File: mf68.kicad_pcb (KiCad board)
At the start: 2 copper layers, 2 parts, among them SW1 MX, U1 nice_nano

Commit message: Arranged a large amount of switches
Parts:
- removed SW1: MX, Keebio-Parts:MX-Alps-Choc-1U
- added D1: D, Diode_THT:D_DO-34_SOD68_P10.16mm_Horizontal, B.Cu at (34.9, -53.2)
- added D10: D, Diode_THT:D_DO-34_SOD68_P10.16mm_Horizontal, B.Cu at (206.4, -53.2)
- added D11: D, Diode_THT:D_DO-34_SOD68_P10.16mm_Horizontal, B.Cu at (225.4, -53.2)
- added D12: D, Diode_THT:D_DO-34_SOD68_P10.16mm_Horizontal, B.Cu at (244.5, -53.2)
- added D13: D, Diode_THT:D_DO-34_SOD68_P10.16mm_Horizontal, B.Cu at (263.5, -53.2)
- added D14: D, Diode_THT:D_DO-34_SOD68_P10.16mm_Horizontal, B.Cu at (42.1, -34.1)
- added D15: D, Diode_THT:D_DO-34_SOD68_P10.16mm_Horizontal, B.Cu at (63.5, -34.1)
- added D16: D, Diode_THT:D_DO-34_SOD68_P10.16mm_Horizontal, B.Cu at (82.5, -34.1)
- added D17: D, Diode_THT:D_DO-34_SOD68_P10.16mm_Horizontal, B.Cu at (101.6, -34.1)
- added D18: D, Diode_THT:D_DO-34_SOD68_P10.16mm_Horizontal, B.Cu at (120.6, -34.1)
- added D19: D, Diode_THT:D_DO-34_SOD68_P10.16mm_Horizontal, B.Cu at (139.7, -34.1)
- added D2: D, Diode_THT:D_DO-34_SOD68_P10.16mm_Horizontal, B.Cu at (54.0, -53.2)
- added D20: D, Diode_THT:D_DO-34_SOD68_P10.16mm_Horizontal, B.Cu at (158.7, -34.1)
- added D21: D, Diode_THT:D_DO-34_SOD68_P10.16mm_Horizontal, B.Cu at (177.8, -34.1)
- added D22: D, Diode_THT:D_DO-34_SOD68_P10.16mm_Horizontal, B.Cu at (196.8, -34.1)
- added D23: D, Diode_THT:D_DO-34_SOD68_P10.16mm_Horizontal, B.Cu at (215.9, -34.1)
- added D24: D, Diode_THT:D_DO-34_SOD68_P10.16mm_Horizontal, B.Cu at (234.9, -34.1)
- added D25: D, Diode_THT:D_DO-34_SOD68_P10.16mm_Horizontal, B.Cu at (254.0, -34.1)
- added D26: D, Diode_THT:D_DO-34_SOD68_P10.16mm_Horizontal, B.Cu at (273.0, -34.1)
- added D27: D, Diode_THT:D_DO-34_SOD68_P10.16mm_Horizontal, B.Cu at (44.4, -15.1)
- added D28: D, Diode_THT:D_DO-34_SOD68_P10.16mm_Horizontal, B.Cu at (68.3, -15.1)
- added D29: D, Diode_THT:D_DO-34_SOD68_P10.16mm_Horizontal, B.Cu at (87.3, -15.1)
- added D3: D, Diode_THT:D_DO-34_SOD68_P10.16mm_Horizontal, B.Cu at (73.8, -53.2)
- added D30: D, Diode_THT:D_DO-34_SOD68_P10.16mm_Horizontal, B.Cu at (106.4, -15.1)
- added D31: D, Diode_THT:D_DO-34_SOD68_P10.16mm_Horizontal, B.Cu at (111.9, -8.73)
- added D32: D, Diode_THT:D_DO-34_SOD68_P10.16mm_Horizontal, F.Cu at (131.0, -11.9)
- added D33: D, Diode_THT:D_DO-34_SOD68_P10.16mm_Horizontal, F.Cu at (150.0, -11.9)
- added D34: D, Diode_THT:D_DO-34_SOD68_P10.16mm_Horizontal, F.Cu at (169.1, -11.9)
- added D35: D, Diode_THT:D_DO-34_SOD68_P10.16mm_Horizontal, F.Cu at (188.1, -11.9)
- added D36: D, Diode_THT:D_DO-34_SOD68_P10.16mm_Horizontal, F.Cu at (207.2, -11.9)
- added D37: D, Diode_THT:D_DO-34_SOD68_P10.16mm_Horizontal, F.Cu at (226.2, -11.9)
- added D38: D, Diode_THT:D_DO-34_SOD68_P10.16mm_Horizontal, F.Cu at (245.3, -11.9)
- added D39: D, Diode_THT:D_DO-34_SOD68_P10.16mm_Horizontal, F.Cu at (276.2, -11.9)
- added D4: D, Diode_THT:D_DO-34_SOD68_P10.16mm_Horizontal, B.Cu at (92.1, -53.2)
- added D40: D, Diode_THT:D_DO-34_SOD68_P10.16mm_Horizontal, F.Cu at (27.0, 5.56)
- added D41: D, Diode_THT:D_DO-34_SOD68_P10.16mm_Horizontal, F.Cu at (63.5, 5.56)
- added D42: D, Diode_THT:D_DO-34_SOD68_P10.16mm_Horizontal, F.Cu at (83.3, 5.56)
- added D43: D, Diode_THT:D_DO-34_SOD68_P10.16mm_Horizontal, F.Cu at (101.6, 5.56)
- added D44: D, Diode_THT:D_DO-34_SOD68_P10.16mm_Horizontal, F.Cu at (120.6, 5.56)
- added D45: D, Diode_THT:D_DO-34_SOD68_P10.16mm_Horizontal, F.Cu at (139.7, 5.56)
- added D46: D, Diode_THT:D_DO-34_SOD68_P10.16mm_Horizontal, F.Cu at (158.7, 5.56)
- added D47: D, Diode_THT:D_DO-34_SOD68_P10.16mm_Horizontal, F.Cu at (177.8, 5.56)
- added D48: D, Diode_THT:D_DO-34_SOD68_P10.16mm_Horizontal, F.Cu at (196.8, 5.56)
- added D49: D, Diode_THT:D_DO-34_SOD68_P10.16mm_Horizontal, F.Cu at (215.9, 5.56)
- added D5: D, Diode_THT:D_DO-34_SOD68_P10.16mm_Horizontal, B.Cu at (111.1, -53.2)
- added D50: D, Diode_THT:D_DO-34_SOD68_P10.16mm_Horizontal, F.Cu at (234.9, 5.56)
- added D51: D, Diode_THT:D_DO-34_SOD68_P10.16mm_Horizontal, F.Cu at (254.0, 5.56)
- added D52: D, Diode_THT:D_DO-34_SOD68_P10.16mm_Horizontal, B.Cu at (280.2, -44.4)
- added D53: D, Diode_THT:D_DO-34_SOD68_P10.16mm_Horizontal, F.Cu at (29.4, 26.2)
- added D54: D, Diode_THT:D_DO-34_SOD68_P10.16mm_Horizontal, F.Cu at (53.2, 26.2)
- added D55: D, Diode_THT:D_DO-34_SOD68_P10.16mm_Horizontal, F.Cu at (77.0, 26.2)
- added D56: D, Diode_THT:D_DO-34_SOD68_P10.16mm_Horizontal, F.Cu at (100.8, 26.2)
- added D57: D, Diode_THT:D_DO-34_SOD68_P10.16mm_Horizontal, F.Cu at (138.9, 26.2)
- added D58: D, Diode_THT:D_DO-34_SOD68_P10.16mm_Horizontal, F.Cu at (179.4, 26.2)
- added D59: D, Diode_THT:D_DO-34_SOD68_P10.16mm_Horizontal, F.Cu at (218.3, 26.2)
- added D6: D, Diode_THT:D_DO-34_SOD68_P10.16mm_Horizontal, B.Cu at (130.2, -53.2)
- added D60: D, Diode_THT:D_DO-34_SOD68_P10.16mm_Horizontal, F.Cu at (241.3, 26.2)
- added D61: D, Diode_THT:D_DO-34_SOD68_P10.16mm_Horizontal, F.Cu at (265.9, 26.2)
- added D62: D, Diode_THT:D_DO-34_SOD68_P10.16mm_Horizontal, F.Cu at (284.9, 26.2)
- added D63: D, Diode_THT:D_DO-34_SOD68_P10.16mm_Horizontal, F.Cu at (304.0, 26.2)
- added D64: D, Diode_THT:D_DO-34_SOD68_P10.16mm_Horizontal, F.Cu at (284.9, 7.14)
- added D65: D, Diode_THT:D_DO-34_SOD68_P10.16mm_Horizontal, F.Cu at (275.4, -54.0)
- added D7: D, Diode_THT:D_DO-34_SOD68_P10.16mm_Horizontal, B.Cu at (149.2, -53.2)
- added D8: D, Diode_THT:D_DO-34_SOD68_P10.16mm_Horizontal, B.Cu at (168.3, -53.2)
- added D9: D, Diode_THT:D_DO-34_SOD68_P10.16mm_Horizontal, B.Cu at (187.3, -53.2)
- added K1: ESC, Keebio-Parts:MX-Alps-Choc-1U-NoLED, F.Cu at (25.4, -59.5)
- added K10: #9, Keebio-Parts:MX-Alps-Choc-1U-NoLED, F.Cu at (196.8, -59.5)
- added K11: #0, Keebio-Parts:MX-Alps-Choc-1U-NoLED, F.Cu at (215.9, -59.5)
- added K12: MINUS, Keebio-Parts:MX-Alps-Choc-1U-NoLED, F.Cu at (234.9, -59.5)
- added K13: PLUS, Keebio-Parts:MX-Alps-Choc-1U-NoLED, F.Cu at (254.0, -59.5)
- added K14: TAB, Keebio-Parts:MX-Alps-Choc-1U-NoLED, F.Cu at (30.2, -40.5)
- added K15: Q, Keebio-Parts:MX-Alps-Choc-1U-NoLED, F.Cu at (54.0, -40.5)
- added K16: W, Keebio-Parts:MX-Alps-Choc-1U-NoLED, F.Cu at (73.0, -40.5)
- added K17: E, Keebio-Parts:MX-Alps-Choc-1U-NoLED, F.Cu at (92.1, -40.5)
- added K18: R, Keebio-Parts:MX-Alps-Choc-1U-NoLED, F.Cu at (111.1, -40.5)
- added K19: T, Keebio-Parts:MX-Alps-Choc-1U-NoLED, F.Cu at (130.2, -40.5)
- added K2: #1, Keebio-Parts:MX-Alps-Choc-1U-NoLED, F.Cu at (44.4, -59.5)
- added K20: Y, Keebio-Parts:MX-Alps-Choc-1U-NoLED, F.Cu at (149.2, -40.5)
- added K21: U, Keebio-Parts:MX-Alps-Choc-1U-NoLED, F.Cu at (168.3, -40.5)
- added K22: I, Keebio-Parts:MX-Alps-Choc-1U-NoLED, F.Cu at (187.3, -40.5)
- added K23: O, Keebio-Parts:MX-Alps-Choc-1U-NoLED, F.Cu at (206.4, -40.5)
- added K24: P, Keebio-Parts:MX-Alps-Choc-1U-NoLED, F.Cu at (225.4, -40.5)
- added K25: [, Keebio-Parts:MX-Alps-Choc-1U-NoLED, F.Cu at (244.5, -40.5)
- added K26: ], Keebio-Parts:MX-Alps-Choc-1U-NoLED, F.Cu at (263.5, -40.5)
- added K27: CAPS, Keebio-Parts:MX-Alps-Choc-1U-NoLED, F.Cu at (34.9, -21.4)
- added K28: A, Keebio-Parts:MX-Alps-Choc-1U-NoLED, F.Cu at (58.7, -21.4)
- added K29: S, Keebio-Parts:MX-Alps-Choc-1U-NoLED, F.Cu at (77.8, -21.4)
- added K3: #2, Keebio-Parts:MX-Alps-Choc-1U-NoLED, F.Cu at (63.5, -59.5)
- added K30: D, Keebio-Parts:MX-Alps-Choc-1U-NoLED, F.Cu at (96.8, -21.4)
- added K31: F, Keebio-Parts:MX-Alps-Choc-1U-NoLED, F.Cu at (115.9, -21.4)
- added K32: G, Keebio-Parts:MX-Alps-Choc-1U-NoLED, F.Cu at (134.9, -21.4)
- added K33: H, Keebio-Parts:MX-Alps-Choc-1U-NoLED, F.Cu at (154.0, -21.4)
- added K34: J, Keebio-Parts:MX-Alps-Choc-1U-NoLED, F.Cu at (173.0, -21.4)
- added K35: K, Keebio-Parts:MX-Alps-Choc-1U-NoLED, F.Cu at (192.1, -21.4)
- added K36: L, Keebio-Parts:MX-Alps-Choc-1U-NoLED, F.Cu at (211.1, -21.4)
- added K37: ;, Keebio-Parts:MX-Alps-Choc-1U-NoLED, F.Cu at (230.2, -21.4)
- added K38: ', Keebio-Parts:MX-Alps-Choc-1U-NoLED, F.Cu at (249.2, -21.4)
- added K39: ENTER, Keebio-Parts:MX-Alps-Choc-1U-NoLED, F.Cu at (281.0, -21.4)
- added K4: #3, Keebio-Parts:MX-Alps-Choc-1U-NoLED, F.Cu at (82.5, -59.5)
- added K40: LSHIFT, Keebio-Parts:MX-Alps-Choc-1U-NoLED, F.Cu at (31.7, -2.38)
- added K41: Z, Keebio-Parts:MX-Alps-Choc-1U-NoLED, F.Cu at (68.3, -2.38)
- added K42: X, Keebio-Parts:MX-Alps-Choc-1U-NoLED, F.Cu at (87.3, -2.38)
- added K43: C, Keebio-Parts:MX-Alps-Choc-1U-NoLED, F.Cu at (106.4, -2.38)
- added K44: V, Keebio-Parts:MX-Alps-Choc-1U-NoLED, F.Cu at (125.4, -2.38)
- added K45: B, Keebio-Parts:MX-Alps-Choc-1U-NoLED, F.Cu at (144.5, -2.38)
- added K46: N, Keebio-Parts:MX-Alps-Choc-1U-NoLED, F.Cu at (163.5, -2.38)
- added K47: M, Keebio-Parts:MX-Alps-Choc-1U-NoLED, F.Cu at (182.6, -2.38)
- added K48: ,, Keebio-Parts:MX-Alps-Choc-1U-NoLED, F.Cu at (201.6, -2.38)
- added K49: ., Keebio-Parts:MX-Alps-Choc-1U-NoLED, F.Cu at (220.6, -2.38)
- added K5: #4, Keebio-Parts:MX-Alps-Choc-1U-NoLED, F.Cu at (101.6, -59.5)
- added K50: /, Keebio-Parts:MX-Alps-Choc-1U-NoLED, F.Cu at (239.7, -2.38)
- added K51: RSHIFT, Keebio-Parts:MX-Alps-Choc-1U-NoLED, F.Cu at (258.7, -2.38)
- added K52: BKSH, Keebio-Parts:MX-Alps-Choc-1U-NoLED, F.Cu at (289.7, -40.5)
- added K53: LCTL, Keebio-Parts:MX-Alps-Choc-1U-NoLED, F.Cu at (34.1, 16.7)
- added K54: LWIN, Keebio-Parts:MX-Alps-Choc-1U-NoLED, F.Cu at (57.9, 16.7)
- added K55: LALT, Keebio-Parts:MX-Alps-Choc-1U-NoLED, F.Cu at (81.8, 16.7)
- added K56: FN2, Keebio-Parts:MX-Alps-Choc-1U-NoLED, F.Cu at (105.6, 16.7)
- added K57: LSPC, Keebio-Parts:MX-Alps-Choc-1U-NoLED, F.Cu at (143.7, 16.7)
- added K58: RSPC, Keebio-Parts:MX-Alps-Choc-1U-NoLED, F.Cu at (184.1, 16.7)
- added K59: RALT, Keebio-Parts:MX-Alps-Choc-1U-NoLED, F.Cu at (223.0, 16.7)
- added K6: #5, Keebio-Parts:MX-Alps-Choc-1U-NoLED, F.Cu at (120.6, -59.5)
- added K60: RGUI, Keebio-Parts:MX-Alps-Choc-1U-NoLED, F.Cu at (246.0, 16.7)
- added K61: LEFT, Keebio-Parts:MX-Alps-Choc-1U-NoLED, F.Cu at (270.7, 16.7)
- added K62: DOWN, Keebio-Parts:MX-Alps-Choc-1U-NoLED, F.Cu at (289.7, 16.7)
- added K63: RIGHT, Keebio-Parts:MX-Alps-Choc-1U-NoLED, F.Cu at (308.7, 16.7)
- added K64: UP, Keebio-Parts:MX-Alps-Choc-1U-NoLED, F.Cu at (289.7, -2.38)
- added K65: BKSPC, Keebio-Parts:MX-Alps-Choc-1U-NoLED, F.Cu at (289.7, -59.5)
- added K7: #6, Keebio-Parts:MX-Alps-Choc-1U-NoLED, F.Cu at (139.7, -59.5)
- added K8: #7, Keebio-Parts:MX-Alps-Choc-1U-NoLED, F.Cu at (158.7, -59.5)
- added K9: #8, Keebio-Parts:MX-Alps-Choc-1U-NoLED, F.Cu at (177.8, -59.5)
- U1: moved to B.Cu
- moved U1 245.2 mm to (311.1, -51.6), turned to 270 degrees
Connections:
- U1 pad 1: (no net) -> row0
- U1 pad 10: (no net) -> col10
- U1 pad 11: (no net) -> col11
- U1 pad 12: (no net) -> col12
- U1 pad 13: (no net) -> col7
- U1 pad 14: (no net) -> col6
- U1 pad 15: (no net) -> col5
- U1 pad 16: (no net) -> col4
- U1 pad 17: (no net) -> col3
- U1 pad 18: (no net) -> col2
- U1 pad 19: (no net) -> col1
- U1 pad 2: (no net) -> row1
- U1 pad 20: (no net) -> col0
- U1 pad 5: (no net) -> row2
- U1 pad 6: (no net) -> row3
- U1 pad 7: (no net) -> row4
- U1 pad 8: (no net) -> col8
- U1 pad 9: (no net) -> col9
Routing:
- net row0: track 0.00 -> 372.1 mm
- net row1: track 0.00 -> 349.4 mm
- net (no net): track 0.00 -> 71.7 mm
- net col0: track 0.00 -> 58.5 mm
- net Net-(D3-Pad2): track 0.00 -> 8.11 mm
- net Net-(D13-Pad2): track 0.00 -> 7.32 mm
- net Net-(D5-Pad2): track 0.00 -> 7.32 mm
- net Net-(D4-Pad2): track 0.00 -> 7.32 mm
- net Net-(D1-Pad2): track 0.00 -> 7.32 mm
- net Net-(D6-Pad2): track 0.00 -> 7.32 mm
- net Net-(D2-Pad2): track 0.00 -> 7.32 mm
- net Net-(D9-Pad2): track 0.00 -> 7.32 mm
- net Net-(D8-Pad2): track 0.00 -> 7.32 mm
- net Net-(D7-Pad2): track 0.00 -> 7.32 mm
- net Net-(D12-Pad2): track 0.00 -> 7.32 mm
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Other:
- net class Default: trace_width 0.25 -> 0.4

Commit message: Wip: row stagger is wrong!
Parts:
- added REF**: 1.25U, MX_Alps_Hybrid:MX-1.25U, F.Cu at (273.0, 148.4)
- added REF**: 1.25U, MX_Alps_Hybrid:MX-1.25U, F.Cu at (249.2, 148.4)
- added REF**: 1.25U, MX_Alps_Hybrid:MX-1.25U, F.Cu at (225.4, 148.4)
- added REF**: 1.25U, MX_Alps_Hybrid:MX-1.25U, F.Cu at (201.6, 148.4)
- added REF**: 1.25U, MX_Alps_Hybrid:MX-1.25U, F.Cu at (58.7, 148.4)
- added REF**: 1.25U, MX_Alps_Hybrid:MX-1.25U, F.Cu at (34.9, 148.4)
- added REF**: 1.25U, MX_Alps_Hybrid:MX-1.25U, F.Cu at (11.1, 148.4)
- added REF**: 6.25U, MX_Alps_Hybrid:MX-6.25U, F.Cu at (130.2, 148.4)
- D32, D33, D34, D35, D36, D37, D38, D39, D40, D41, D42, D43, D44, D45, D46, D47, D48, D49, D50, D51, D53, D54, D55, D56, D57, D58, D59, D60, D61, D62, D63, D64, D65: moved to B.Cu
- K39, K57, K58: footprint Keebio-Parts:MX-Alps-Choc-1U-NoLED -> Keebio-Parts:MX-Alps-Choc-2U
- K40: footprint Keebio-Parts:MX-Alps-Choc-1U-NoLED -> xeal_components:MX-Alps-Choc-2U-pin-flip
- K61, K62, K63: footprint Keebio-Parts:MX-Alps-Choc-1U-NoLED -> xeal_components:MX-Alps-Choc-1U-NoLED-PinSwap
- K65: footprint Keebio-Parts:MX-Alps-Choc-1U-NoLED -> xeal_components:MX-Alps-Choc-2U-no-led
- moved K57 116.1 mm to (115.9, 129.4), turned to 180 degrees
- moved K53 115.0 mm to (11.1, 129.4)
- moved K54 115.0 mm to (34.9, 129.4)
- moved K55 115.0 mm to (58.7, 129.4)
- moved K56 115.0 mm to (82.5, 129.4)
- moved K59 114.7 mm to (201.6, 129.4)
- moved K65 114.7 mm to (268.3, 53.2)
- moved K58 114.6 mm to (163.5, 129.4), turned to 180 degrees
- moved K60 114.6 mm to (225.4, 129.4)
- moved K39 113.7 mm to (265.9, 91.3)
- moved D65 113.6 mm to (251.6, 57.1)
- moved K1 113.6 mm to (11.1, 53.2)
- moved K10 113.6 mm to (182.6, 53.2)
- moved K11 113.6 mm to (201.6, 53.2)
- moved K12 113.6 mm to (220.6, 53.2)
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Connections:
- U1 pad 1: row0 -> row1
- U1 pad 10: col10 -> col12
- U1 pad 12: col12 -> row3
- U1 pad 13: col7 -> col6
- U1 pad 14: col6 -> col5
- U1 pad 15: col5 -> col4
- U1 pad 16: col4 -> col3
- U1 pad 17: col3 -> col2
- U1 pad 18: col2 -> col1
- U1 pad 19: col1 -> col0
- U1 pad 2: row1 -> col7
- U1 pad 20: col0 -> row0
- U1 pad 6: row3 -> col8
- U1 pad 7: row4 -> col9
- U1 pad 8: col8 -> col10
- U1 pad 9: col9 -> row4
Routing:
- net row4: track 0.00 -> 504.2 mm, vias 0 -> 1
- net row3: track 0.00 -> 399.4 mm
- net col1: track 0.00 -> 384.1 mm
- net col2: track 0.00 -> 358.3 mm, vias 0 -> 1
- net col7: track 0.00 -> 349.0 mm
- net row2: track 0.00 -> 343.8 mm, vias 0 -> 1
- net col3: track 0.00 -> 336.9 mm, vias 0 -> 1
- net col8: track 0.00 -> 330.5 mm
- net col4: track 0.00 -> 328.1 mm, vias 0 -> 1
- net col6: track 0.00 -> 325.4 mm, vias 0 -> 1
- net col5: track 0.00 -> 319.6 mm, vias 0 -> 1
- net col0: track 58.5 -> 376.5 mm
- net col9: track 0.00 -> 310.9 mm
- net col10: track 0.00 -> 291.8 mm
- net col12: track 0.00 -> 189.2 mm
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
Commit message: wip: Row stagger fixed for ansi
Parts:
- removed the REF** at (273.0, 148.4)
- removed the REF** at (249.2, 148.4)
- removed the REF** at (225.4, 148.4)
- removed the REF** at (201.6, 148.4)
- removed the REF** at (58.7, 148.4)
- removed the REF** at (34.9, 148.4)
- added REF**: 1.75U, MX_Alps_Hybrid:MX-1.75U, F.Cu at (251.6, 110.3)
- added REF**: 1.25U, MX_Alps_Hybrid:MX-1.25U, F.Cu at (37.3, 148.4)
- added REF**: 1.5U, MX_Alps_Hybrid:MX-1.5U, F.Cu at (65.1, 185.7)
- added REF**: 1.5U, MX_Alps_Hybrid:MX-1.5U, F.Cu at (36.5, 185.7)
- added REF**: 1.25U, MX_Alps_Hybrid:MX-1.25U, F.Cu at (10.3, 185.7)
- added REF**: 1.25U, MX_Alps_Hybrid:MX-1.25U, F.Cu at (275.4, 148.4)
- added REF**: 1.25U, MX_Alps_Hybrid:MX-1.25U, F.Cu at (251.6, 148.4)
- added REF**: 1.25U, MX_Alps_Hybrid:MX-1.25U, F.Cu at (227.8, 148.4)
- added REF**: 1.25U, MX_Alps_Hybrid:MX-1.25U, F.Cu at (204.0, 148.4)
- added REF**: 1.25U, MX_Alps_Hybrid:MX-1.25U, F.Cu at (61.1, 148.4)
- moved K40 4.76 mm to (23.0, 110.3)
- moved D40 2.38 mm to (39.7, 114.3)
- moved D52 2.38 mm to (263.5, 65.9)
- moved D55 2.38 mm to (70.6, 133.3)
- moved D56 2.38 mm to (94.5, 133.3)
- moved D57 2.38 mm to (134.9, 134.1)
- moved D59 2.38 mm to (213.5, 133.3)
- moved D60 2.38 mm to (237.3, 133.2)
- moved D61 2.38 mm to (249.2, 133.2)
- moved D62 2.38 mm to (268.3, 133.3)
- moved K56 2.38 mm to (84.9, 129.4)
- moved K57 2.38 mm to (118.3, 129.4)
- moved K58 2.38 mm to (165.9, 129.4)
- moved K59 2.38 mm to (204.0, 129.4)
- moved K60 2.38 mm to (227.8, 129.4)
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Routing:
- net col0: track 376.5 -> 386.2 mm
- net Net-(D14-Pad2): track 10.7 -> 18.2 mm
- net col1: track 384.1 -> 391.6 mm
- net Net-(D52-Pad2): track 27.2 -> 34.2 mm
- net col9: track 310.9 -> 314.5 mm
- net col8: track 330.5 -> 334.1 mm
- net col6: track 325.4 -> 327.8 mm
- net Net-(D27-Pad2): track 8.30 -> 10.7 mm
- net Net-(D40-Pad2): track 17.8 -> 15.4 mm
- net row4: track 504.2 -> 506.6 mm
- net col5: track 319.6 -> 322.0 mm
- net col10: track 291.8 -> 293.7 mm
- net Net-(D64-Pad2): track 8.04 -> 6.24 mm
- net col3: track 336.9 -> 335.3 mm
- net col12: track 189.2 -> 187.8 mm
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
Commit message: Fixed annotations, Only missing battery dip switch
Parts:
- removed REF**: 1.75U, MX_Alps_Hybrid:MX-1.75U
- removed REF** (x8): 1.25U, MX_Alps_Hybrid:MX-1.25U
- removed REF**: 6.25U, MX_Alps_Hybrid:MX-6.25U
- removed REF** (x2): 1.5U, MX_Alps_Hybrid:MX-1.5U
- added POWER_SW1: SW_SPDT, Button_Switch_THT:SW_E-Switch_EG1224_SPDT_Angled, F.Cu at (279.4, 35.6)
- D1, D10, D11, D12, D13, D14, D15, D16, D17, D18, D19, D2, D20, D21, D22, D23, D24, D25, D26, D27, D28, D29, D3, D30, D31, D32, D33, D34, D35, D36, D37, D38, D39, D4, D40, D41, D42, D43, D44, D45, D46, D47, D48, D49, D5, D50, D51, D52, D53, D54, D55, D56, D57, D58, D59, D6, D60, D61, D62, D63, D64, D65, D7, D8, D9: footprint Diode_THT:D_DO-34_SOD68_P10.16mm_Horizontal -> xeal_components:D_DO-34_SOD68_P10.16mm_Horizontal_NoK
- K1, K10, K11, K12, K13, K14, K15, K16, K17, K18, K19, K2, K20, K21, K22, K23, K24, K25, K26, K27, K28, K29, K3, K30, K31, K32, K33, K34, K35, K36, K4, K41, K42, K43, K44, K45, K46, K47, K5, K51, K53, K55, K56, K59, K6, K60, K64, K7, K8, K9: footprint Keebio-Parts:MX-Alps-Choc-1U-NoLED -> xeal_components:MX-Choc-1U
- K37: value ; -> SEMICOLON; footprint Keebio-Parts:MX-Alps-Choc-1U-NoLED -> xeal_components:MX-Choc-1U
- K38: value ' -> QUOTE; footprint Keebio-Parts:MX-Alps-Choc-1U-NoLED -> xeal_components:MX-Choc-1U
- K39, K57, K58: footprint Keebio-Parts:MX-Alps-Choc-2U -> xeal_components:MX-Alps-Choc-2U-no-led
- K48: value , -> COMMA; footprint Keebio-Parts:MX-Alps-Choc-1U-NoLED -> xeal_components:MX-Choc-1U
- K49: value . -> DOT; footprint Keebio-Parts:MX-Alps-Choc-1U-NoLED -> xeal_components:MX-Choc-1U
- K50: value / -> SLASH; footprint Keebio-Parts:MX-Alps-Choc-1U-NoLED -> xeal_components:MX-Choc-1U
- K52: value BKSH -> BACKSLASH; footprint Keebio-Parts:MX-Alps-Choc-1U-NoLED -> xeal_components:MX-Choc-1U
- K54: value LWIN -> LGUI; footprint Keebio-Parts:MX-Alps-Choc-1U-NoLED -> xeal_components:MX-Choc-1U
- K61, K62, K63: footprint xeal_components:MX-Alps-Choc-1U-NoLED-PinSwap -> xeal_components:MX-Choc-1U-pin-flip
- moved D64 18.2 mm to (266.7, 114.3)
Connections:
- U1 pad 23: (no net) -> Net-(POWER_SW1-Pad2)
- U1 pad 24: (no net) -> Net-(POWER_SW1-Pad1)
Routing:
- net row4: track 506.6 -> 531.4 mm
- net row3: track 398.6 -> 378.2 mm, vias 0 -> 1
- net Net-(D64-Pad2): track 6.24 -> 18.3 mm
- net col0: track 386.2 -> 393.7 mm
- net col4: track 329.1 -> 336.6 mm
- net col8: track 334.1 -> 340.0 mm
- net col2: track 359.5 -> 364.9 mm
- net col3: track 335.3 -> 339.8 mm
- net col12: track 187.8 -> 191.3 mm, vias 0 -> 2
- net col9: track 314.5 -> 317.8 mm
- net col1: track 391.6 -> 394.1 mm
- net col6: track 327.8 -> 330.0 mm
- net col10: track 293.7 -> 295.2 mm
- net col7: track 348.4 -> 349.9 mm
- net col5: track 322.0 -> 323.2 mm
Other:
- board outline added: 312.4 x 101.6 mm

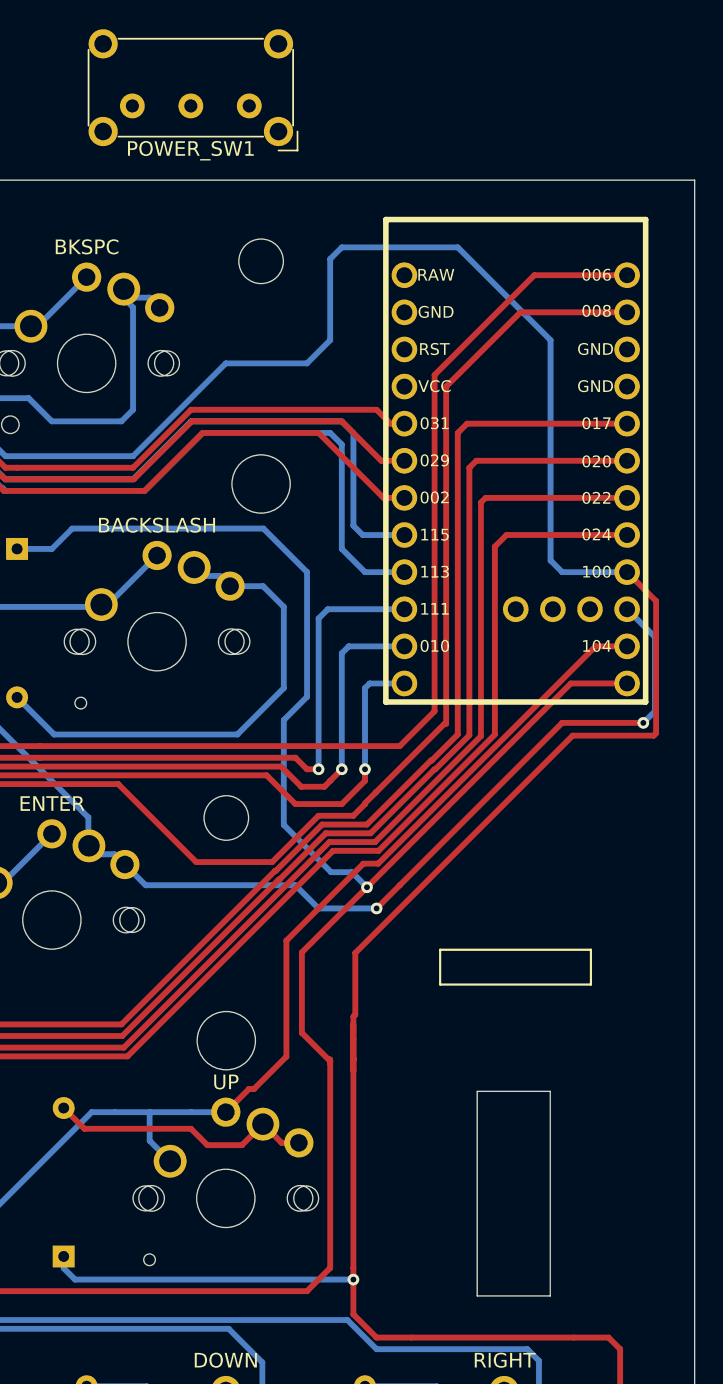
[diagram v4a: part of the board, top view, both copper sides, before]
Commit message: new: Add footprint for microswitch and battery
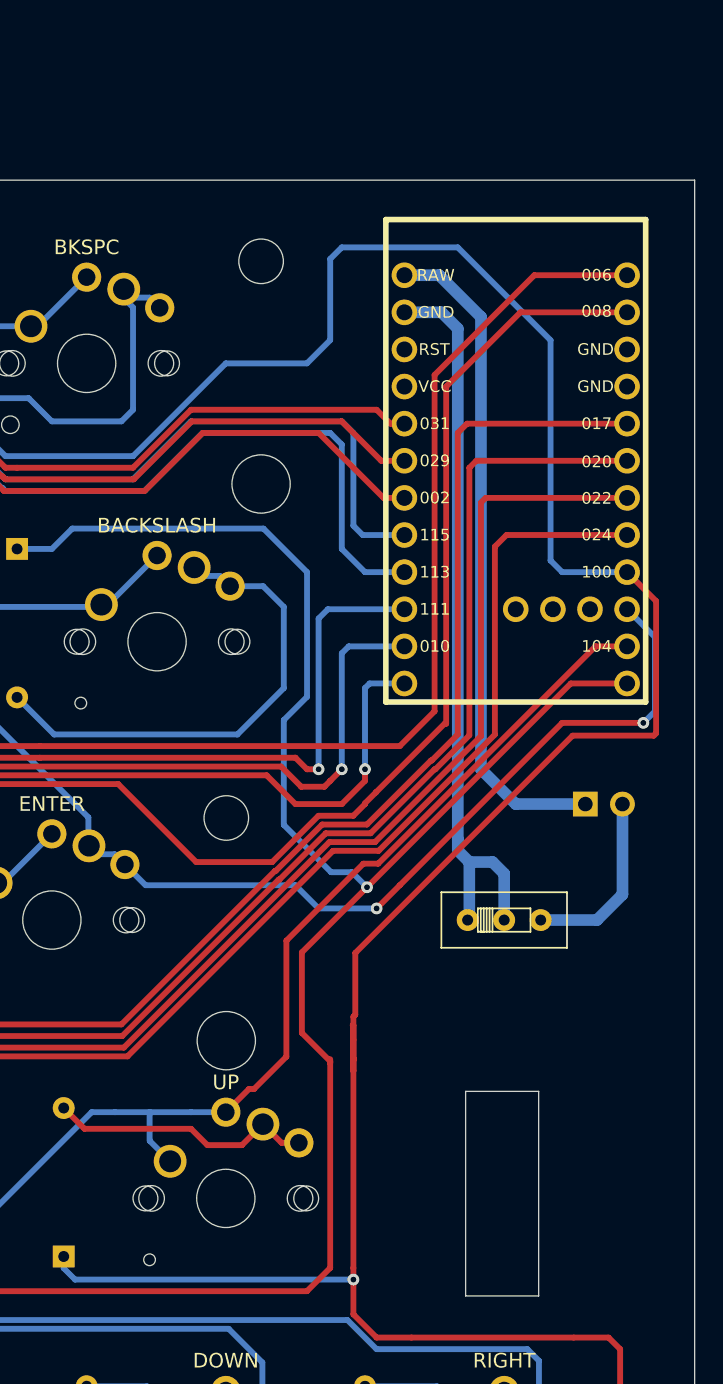
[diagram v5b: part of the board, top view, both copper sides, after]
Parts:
- added BT1: Battery, Connector_PinSocket_2.54mm:PinSocket_1x02_P2.54mm_Vertical, B.Cu at (302.4, 83.3)
- POWER_SW1: footprint Button_Switch_THT:SW_E-Switch_EG1224_SPDT_Angled -> xeal_components:SS12D00
- moved POWER_SW1 58.4 mm to (296.8, 91.3), turned to 0 degrees
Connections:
- POWER_SW1 pad 2: Net-(POWER_SW1-Pad2) -> Net-(POWER_SW1-Pad1)
- POWER_SW1 pad 3: Net-(POWER_SW1-Pad2) -> Net-(BT1-Pad2)
- U1 pad 23: Net-(POWER_SW1-Pad2) -> Net-(POWER_SW1-Pad1)
- U1 pad 24: Net-(POWER_SW1-Pad1) -> Net-(BT1-Pad1)
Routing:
- net Net-(POWER_SW1-Pad1): track 0.00 -> 50.9 mm
- net Net-(BT1-Pad1): track 0.00 -> 45.5 mm
- net Net-(BT1-Pad2): track 0.00 -> 12.5 mm
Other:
- outline, holes or cut-outs redrawn
- net class POWER added: clearance 0.2, trace_width 0.8, via_dia 0.8, via_drill 0.4
- board text added: "B+"
- board text added: "B-"

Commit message: Update labels on footprints
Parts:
- K14, K51, K52, K53, K54, K55: footprint xeal_components:MX-Choc-1U -> xeal_components:MX-Choc-1.5U
- K27: footprint xeal_components:MX-Choc-1U -> xeal_components:MX-Alps-Choc-2U-pin-flip
- K40: footprint xeal_components:MX-Alps-Choc-2U-pin-flip -> xeal_components:MX-Choc-2.5U-pin21
- K56: footprint xeal_components:MX-Choc-1U -> xeal_components:MX-Alps-Choc-2U-stabflip-pinflip
- K57, K58: footprint xeal_components:MX-Alps-Choc-2U-no-led -> xeal_components:MX-Alps-Choc-2U-stabflip-pinflip
- moved D56 27.8 mm to (122.2, 133.3)
- moved D57 26.2 mm to (161.1, 133.2)
- moved K57 26.2 mm to (144.5, 129.4), turned to 0 degrees
- moved K56 21.4 mm to (106.4, 129.4)
- moved D58 16.7 mm to (199.2, 133.3)
- moved K58 16.7 mm to (182.6, 129.4), turned to 0 degrees
- moved K55 11.9 mm to (73.0, 129.4)
- moved D55 11.9 mm to (82.5, 133.3)
- moved K59 7.14 mm to (211.1, 129.4)
- moved D54 7.14 mm to (54.0, 133.3)
- moved K54 7.14 mm to (44.4, 129.4)
- moved D59 7.14 mm to (220.6, 133.3)
- moved D29 4.76 mm to (77.8, 95.2)
- moved D30 4.76 mm to (96.8, 95.2)
- moved D31 4.76 mm to (115.9, 95.2)
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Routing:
- net row4: track 531.4 -> 469.7 mm
- net col3: track 339.8 -> 352.0 mm
- net col4: track 336.6 -> 347.4 mm
- net col5: track 323.2 -> 333.8 mm
- net col1: track 394.1 -> 384.0 mm
- net col0: track 393.7 -> 402.4 mm
- net col10: track 295.2 -> 286.7 mm
- net col8: track 340.0 -> 331.4 mm
- net row3: track 378.2 -> 386.0 mm
- net col6: track 330.0 -> 322.7 mm
- net col7: track 349.9 -> 343.0 mm
- net Net-(D56-Pad2): track 8.30 -> 14.9 mm
- net row2: track 343.8 -> 349.9 mm
- net Net-(D58-Pad2): track 21.7 -> 16.0 mm
- net col9: track 317.8 -> 312.4 mm
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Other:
- board size 312.4 x 101.6 mm -> 308 x 95.2 mm
- board text added: "Off"
- board text added: "On"

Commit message: Update MCU postion
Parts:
- moved U1 35.6 mm to (329.0, 77.9)
- moved D63 35.4 mm to (318.7, 149.8)
- moved K57 35.4 mm to (175.8, 145.9)
- moved K58 35.4 mm to (213.9, 145.9)
- moved D13 35.4 mm to (280.6, 73.6)
- moved D20 35.4 mm to (175.8, 92.7)
- moved D21 35.4 mm to (194.8, 92.7)
- moved D22 35.4 mm to (213.9, 92.7)
- moved D23 35.4 mm to (232.9, 92.7)
- moved D24 35.4 mm to (252.0, 92.7)
- moved D25 35.4 mm to (271.0, 92.7)
- moved D38 35.4 mm to (281.4, 111.7)
- moved D39 35.4 mm to (283.7, 111.7)
- moved D45 35.4 mm to (175.8, 130.8)
- moved D46 35.4 mm to (194.8, 130.8)
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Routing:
- net col3: track 352.0 -> 353.3 mm
- net row4: track 469.7 -> 470.9 mm
- net row0: track 303.8 -> 304.9 mm
- net row1: track 328.3 -> 329.2 mm
- net col7: track 343.0 -> 343.7 mm
- net Net-(POWER_SW1-Pad1): track 50.9 -> 50.3 mm
- net col9: track 312.4 -> 311.8 mm
- net col5: track 333.8 -> 333.2 mm
- net col6: track 322.7 -> 322.1 mm

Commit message: Export for jlcpcb
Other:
- board text added: "JLCJLCJLCJLC"
- board text added: "XeaL's MF65-LP"
